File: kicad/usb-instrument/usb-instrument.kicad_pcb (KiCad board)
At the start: 4 copper layers, 100 x 100 mm, 74 parts, among them J1 USB_B_Micro, J2 USB_C_Receptacle_USB2.0_14P, Q5 BS170, Q6 BSS84, Q7 BS170, Q8 BS170, U1 XIAO-ESP32-C3-DIP, U12 LM321, U13 LM321, U2 ADS131M02IRUKR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

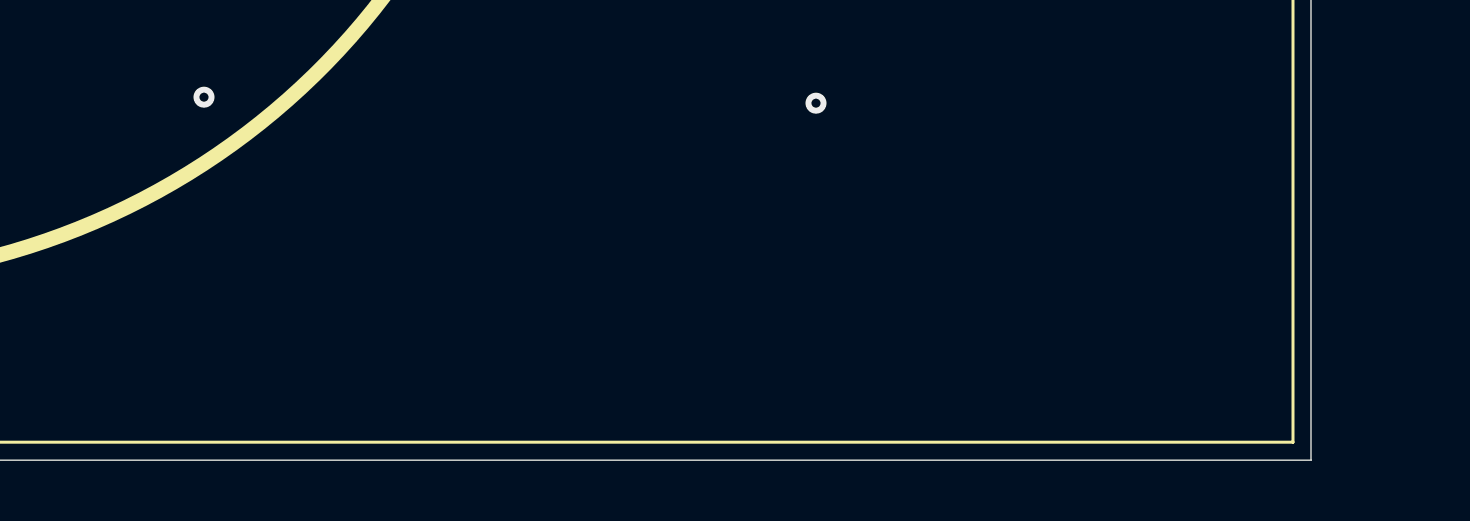
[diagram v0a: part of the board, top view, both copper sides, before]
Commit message: added Title & Rev
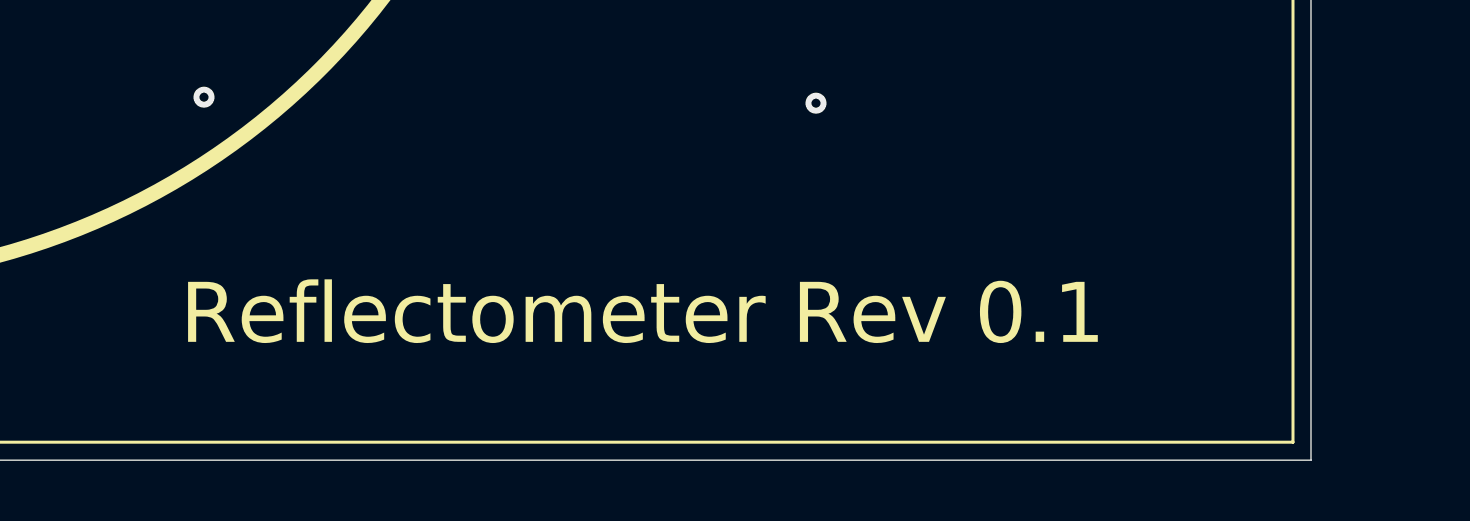
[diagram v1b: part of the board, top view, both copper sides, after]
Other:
- board text added: "Reflectometer Rev 0.1"
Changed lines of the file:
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@@
 	)
 	(paper "A4")
+	(title_block
+		(title "Reflectometer")
+		(rev "0.1")
+		(company "HAW-Hamburg")
+	)
 	(layers
 		(0 "F.Cu" signal)
@@
 		(layer "Edge.Cuts")
 	)
+	(gr_text "Reflectometer Rev 0.1"
+		(at 112.3 146.3 0)
+		(layer "F.SilkS")
+		(effects
+			(font
+				(size 2 2)
+				(thickness 0.2)
+			)
+			(justify left bottom)
+		)
+	)
 	(segment
